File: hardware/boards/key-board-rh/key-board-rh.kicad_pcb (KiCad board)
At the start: 2 copper layers, 106.9 x 42 mm, 32 parts, among them J1 12-way, SW1 KS-33, SW2 KS-33, SW3 KS-33, SW4 KS-33, SW5 KS-33, SW6 KS-33, U1 74HCS165

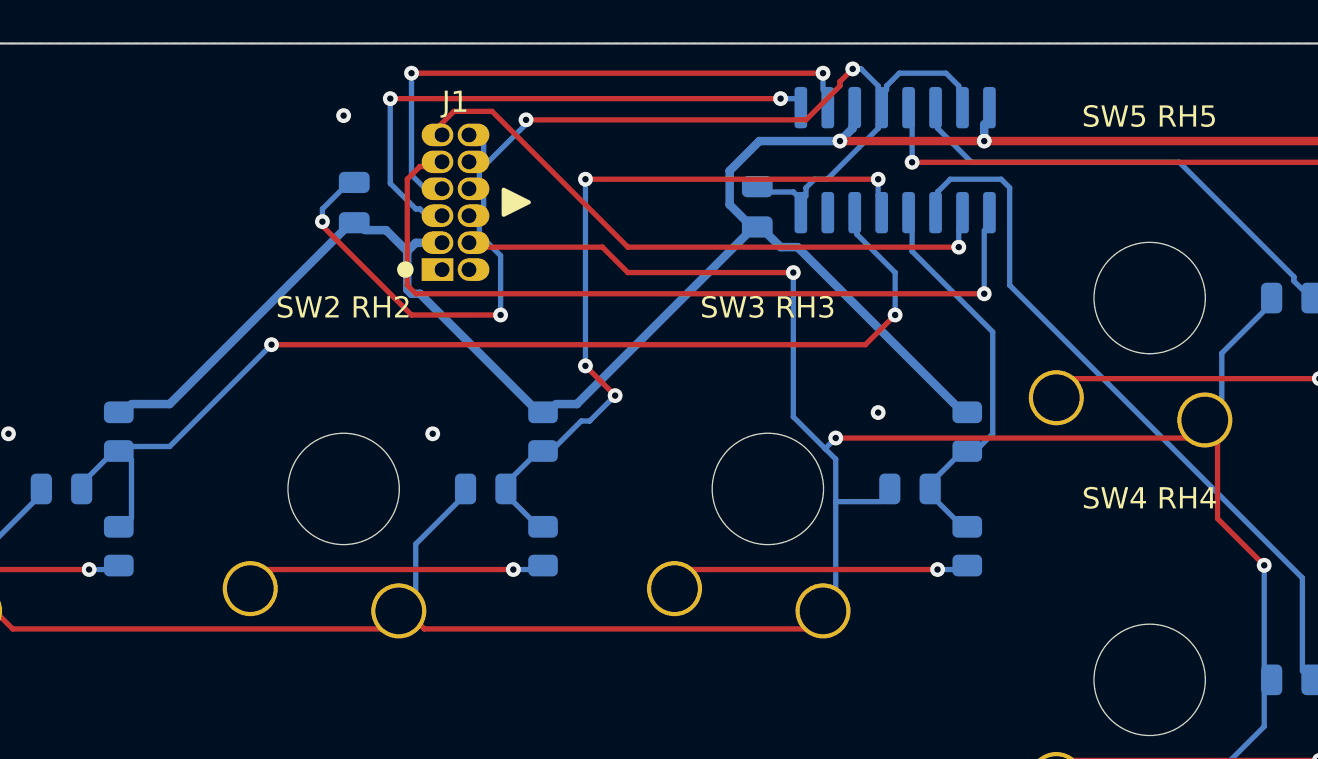
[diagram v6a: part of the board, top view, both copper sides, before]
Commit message: Key board RH laid out again with J-CHAIN 0.5 mm toward the mouth
The chain header follows chain_x (190.0); C8 follows J-CHAIN's 3V3 pin
(178.0). Every net routes on the first pass with the existing route_first
order and the one passive pattern on all six keys; pcb.py check 0 errors
on both key boards. Renders and fab/ re-exported. On the main board J5's
courtyard now clears SW8's pin-1 stub by 0.655 mm against the placement
rule's 0.2 (was 0.155).

Co-Authored-By: Claude Opus 5.5 <noreply@anthropic.com>
Claude-Session: https://claude.ai/code/session_01LmB4muFXnoLprWX4JzuJ5A
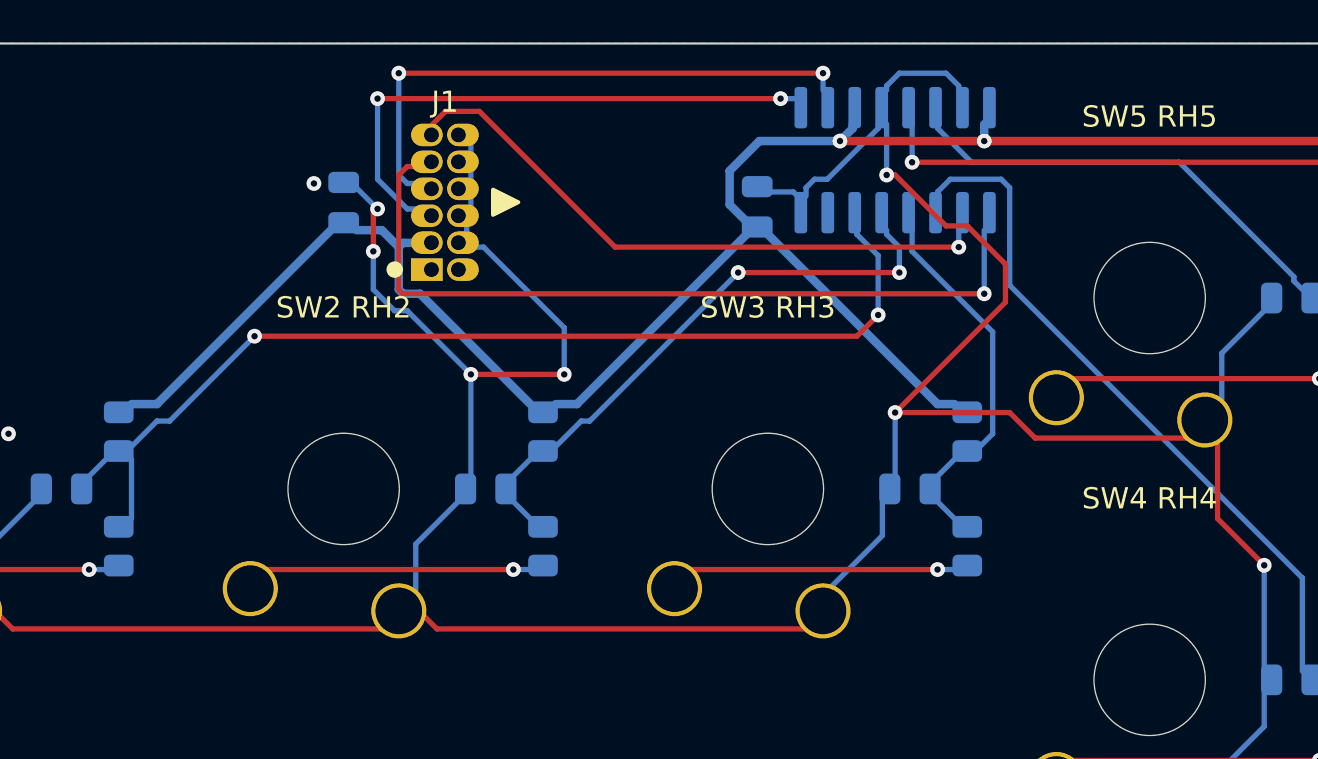
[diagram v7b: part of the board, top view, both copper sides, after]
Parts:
- moved C8 0.50 mm to (238.0, 108.0)
- moved J1 0.50 mm to (242.1, 111.2)
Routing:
- net GND_CHAIN: track 189.8 -> 172.2 mm, vias 12 -> 10
- net /KEY_RH2: track 31.4 -> 24.1 mm, vias 4 -> 2
- net /KEY_RH1: track 47.2 -> 46.1 mm
- net /HOP_LT_RH: track 25.8 -> 26.6 mm
- net /CHAIN_SHLD: track 36.4 -> 37.0 mm
- net /HOP_RH_RT: track 25.4 -> 26.0 mm
